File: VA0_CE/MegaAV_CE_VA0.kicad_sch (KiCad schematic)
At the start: 154 parts, among them CN1 MD-90SM_MD2, IC1 CXA1645/CXA2075/BH7236AF, P1 SMD_Conn_01x01, U2 NCV8114ASN250T1G, U3 TS924, U6 TS922, U7 TS924

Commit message: MegaAV VA0 CE PCBA updates
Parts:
- U3, U7: footprint Package_SO:TSSOP-14_4.4x5mm_P0.65mm -> Package_SO:SO-14_3.9x8.65mm_P1.27mm
- U6: footprint Package_SO:TSSOP-8_4.4x3mm_P0.65mm -> Package_SO:SO-8_3.9x4.9mm_P1.27mm
- renumbered REGION1 to REGION
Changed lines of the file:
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@@
 			)
 		)
-		(property "Footprint" "Package_SO:TSSOP-8_4.4x3mm_P0.65mm"
+		(property "Footprint" "Package_SO:SO-8_3.9x4.9mm_P1.27mm"
 			(at 320.04 133.35 0)
 			(effects
@@
 			)
 		)
-		(property "Footprint" "Package_SO:TSSOP-14_4.4x5mm_P0.65mm"
+		(property "Footprint" "Package_SO:SO-14_3.9x8.65mm_P1.27mm"
 			(at 119.38 193.04 0)
 			(effects
@@
 			)
 		)
-		(property "Footprint" "Package_SO:TSSOP-14_4.4x5mm_P0.65mm"
+		(property "Footprint" "Package_SO:SO-14_3.9x8.65mm_P1.27mm"
 			(at 196.85 156.21 0)
 			(effects
@@
 			)
 		)
-		(property "Footprint" "Package_SO:TSSOP-14_4.4x5mm_P0.65mm"
+		(property "Footprint" "Package_SO:SO-14_3.9x8.65mm_P1.27mm"
 			(at 247.65 242.57 0)
 			(effects
@@
 			)
 		)
-		(property "Footprint" "Package_SO:TSSOP-14_4.4x5mm_P0.65mm"
+		(property "Footprint" "Package_SO:SO-14_3.9x8.65mm_P1.27mm"
 			(at 260.35 242.57 0)
 			(effects
@@
 			)
 		)
-		(property "Footprint" "Package_SO:TSSOP-14_4.4x5mm_P0.65mm"
+		(property "Footprint" "Package_SO:SO-14_3.9x8.65mm_P1.27mm"
 			(at 279.4 165.1 0)
 			(effects
@@
 			)
 		)
-		(property "Footprint" "Package_SO:TSSOP-14_4.4x5mm_P0.65mm"
+		(property "Footprint" "Package_SO:SO-14_3.9x8.65mm_P1.27mm"
 			(at 255.27 153.67 0)
 			(effects
@@
 			)
 		)
-		(property "Footprint" "Package_SO:TSSOP-8_4.4x3mm_P0.65mm"
+		(property "Footprint" "Package_SO:SO-8_3.9x4.9mm_P1.27mm"
 			(at 233.68 242.57 0)
 			(effects
@@
 			)
 		)
-		(property "Footprint" "Package_SO:TSSOP-14_4.4x5mm_P0.65mm"
+		(property "Footprint" "Package_SO:SO-14_3.9x8.65mm_P1.27mm"
 			(at 255.27 181.61 0)
 			(effects
@@
 			)
 		)
-		(property "Footprint" "Package_SO:TSSOP-8_4.4x3mm_P0.65mm"
+		(property "Footprint" "Package_SO:SO-8_3.9x4.9mm_P1.27mm"
 			(at 320.04 105.41 0)
 			(effects
@@
 			)
 		)
-		(property "Footprint" "Package_SO:TSSOP-14_4.4x5mm_P0.65mm"
+		(property "Footprint" "Package_SO:SO-14_3.9x8.65mm_P1.27mm"
 			(at 196.85 184.15 0)
 			(effects
@@
 			)
 		)
-		(property "Footprint" "Package_SO:TSSOP-14_4.4x5mm_P0.65mm"
+		(property "Footprint" "Package_SO:SO-14_3.9x8.65mm_P1.27mm"
 			(at 238.76 215.9 0)
 			(effects
@@
 			)
 		)
-		(property "Footprint" "Package_SO:TSSOP-14_4.4x5mm_P0.65mm"
+		(property "Footprint" "Package_SO:SO-14_3.9x8.65mm_P1.27mm"
 			(at 118.11 148.59 0)
 			(effects
@@
 		(on_board yes)
 		(dnp no)
-		(property "Reference" "REGION1"
+		(property "Reference" "REGION"
 			(at 124.8295 87.2786 0)
 			(effects
@@
 			(project "MegaAV_CE"
 				(path "/672e6c7a-d310-45d1-a117-69a32c775d0f"
-					(reference "REGION1")
+					(reference "REGION")
 					(unit 1)
 				)

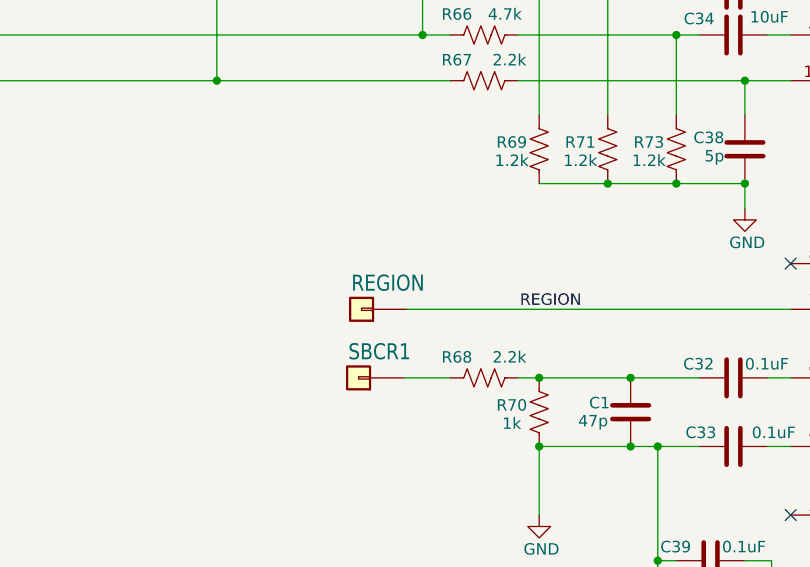
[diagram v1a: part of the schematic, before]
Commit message: Fixed VA0 errors
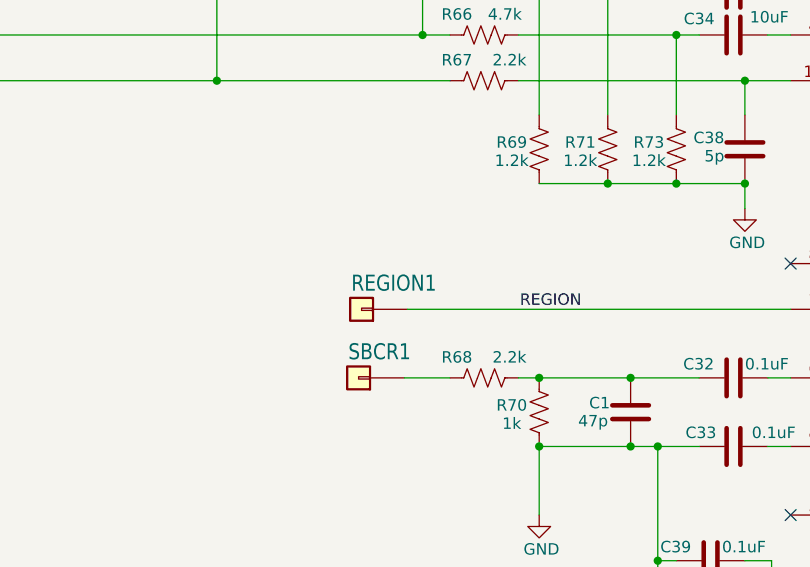
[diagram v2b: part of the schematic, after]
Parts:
- D2: footprint Diode_SMD:D_SOD-882 -> Diode_SMD:D_SOD-323
- renumbered REGION to REGION1
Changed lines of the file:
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@@
 			)
 		)
-		(property "Footprint" "Diode_SMD:D_SOD-882"
+		(property "Footprint" "Diode_SMD:D_SOD-323"
 			(at 318.9958 204.126 0)
 			(effects
@@
 		(on_board yes)
 		(dnp no)
-		(property "Reference" "REGION"
+		(property "Reference" "REGION1"
 			(at 124.8295 87.2786 0)
 			(effects
@@
 			(project "MegaAV_CE"
 				(path "/672e6c7a-d310-45d1-a117-69a32c775d0f"
-					(reference "REGION")
-					(unit 1)
-				)
+					(reference "REGION1")
+					(unit 1)
+				)
